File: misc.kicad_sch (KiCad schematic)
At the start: 12 parts, among them SW2001 SW_435441019830_SMD, SW2002 SW_435441019830_SMD, SW2003 SW_435441019830_SMD

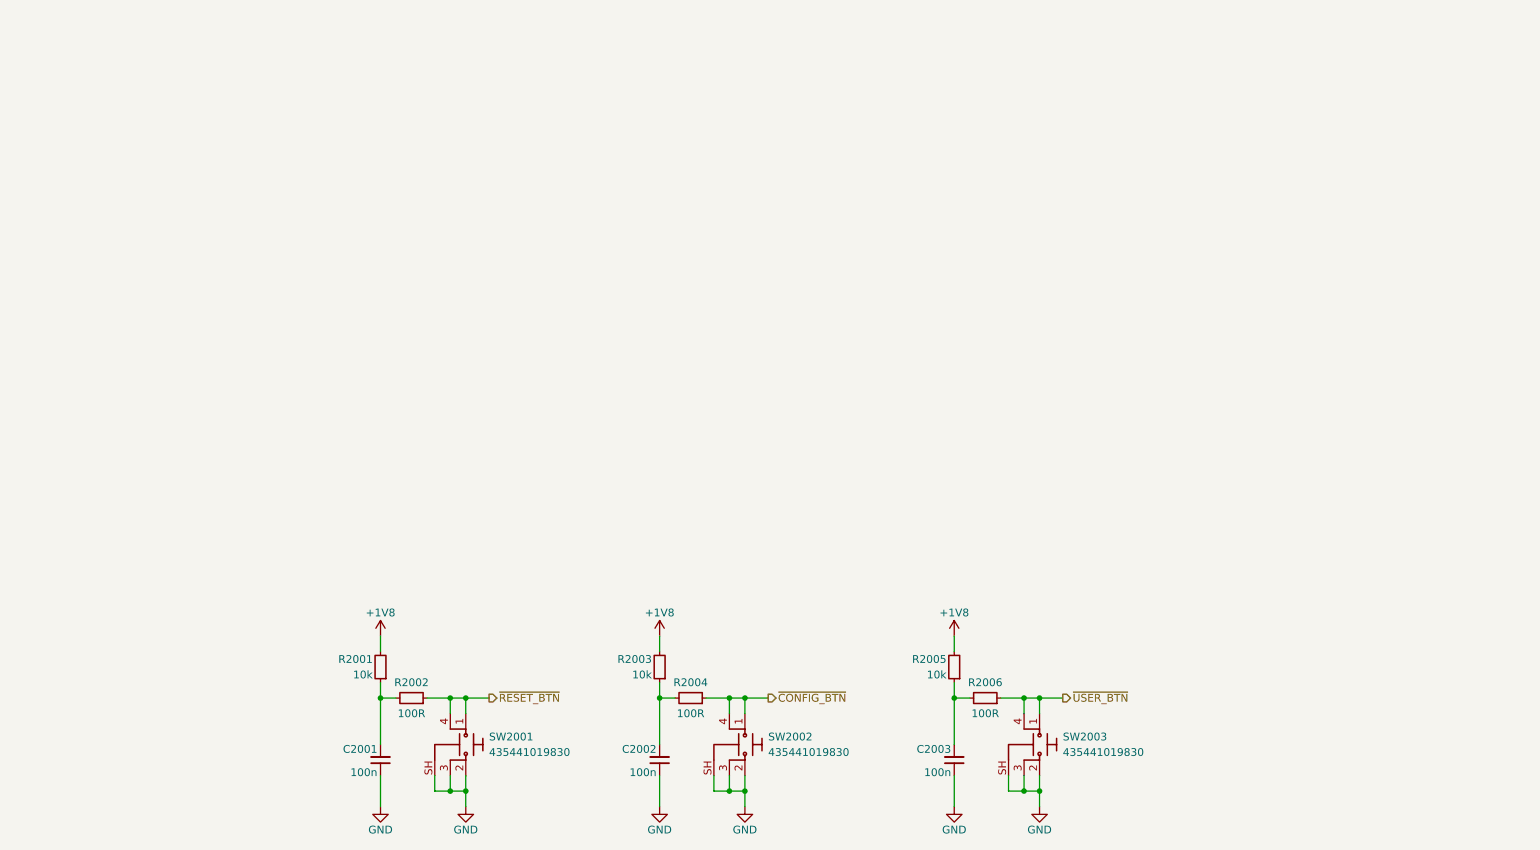
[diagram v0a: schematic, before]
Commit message: [#100125] Add DEBUG buttons, connect BIOS on root schematic
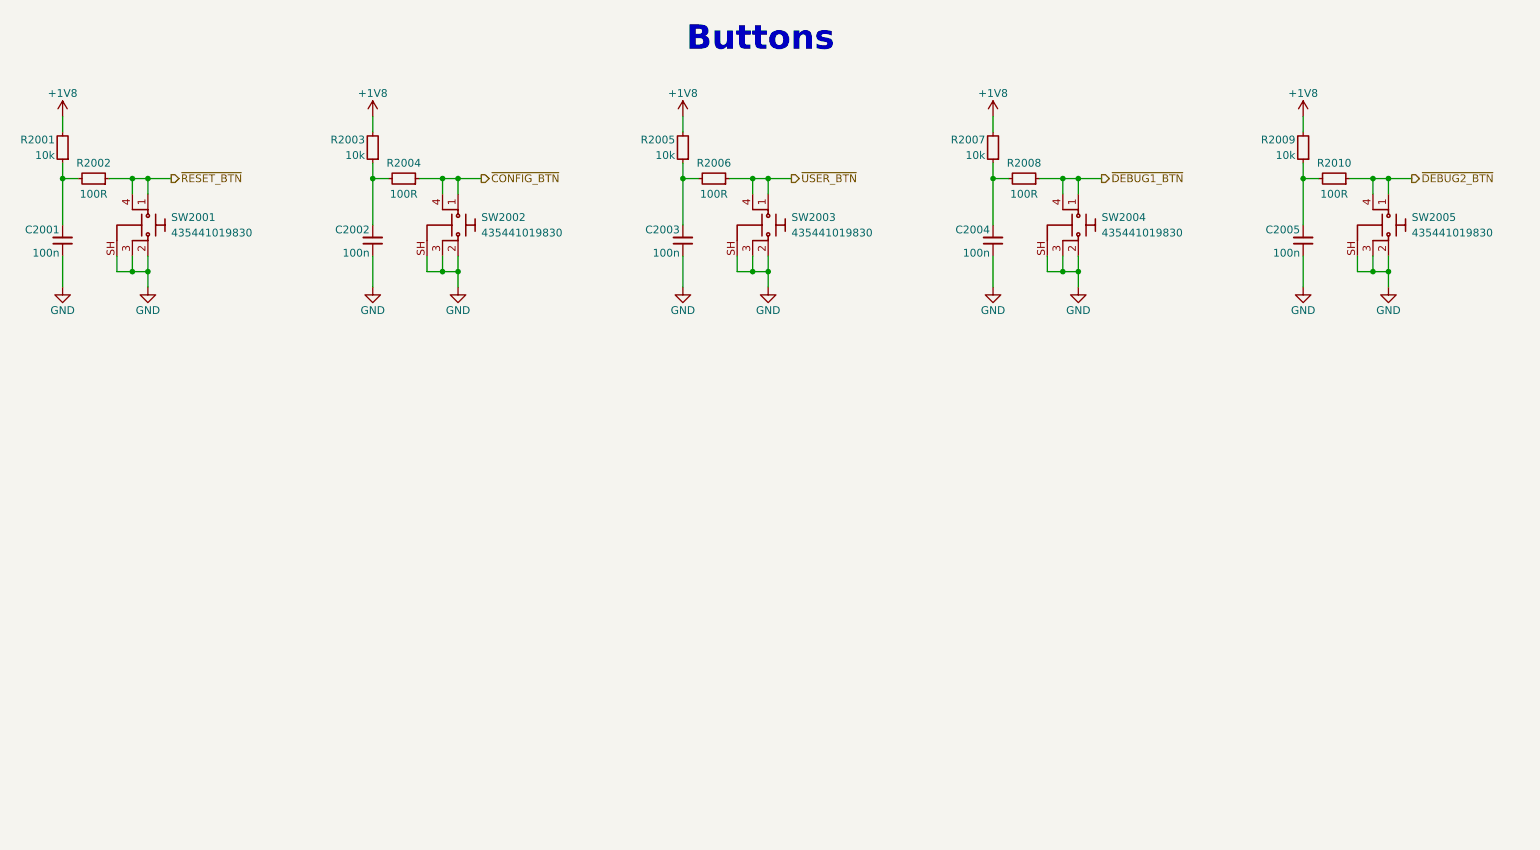
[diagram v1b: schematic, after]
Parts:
- added C2004, C2005: C_100n_0402, antmicro-footprints:C_0402_1005Metric, symbol antmicroCapacitors0402:C_100n_0402
- added R2007, R2009: R_10k_0402, antmicro-footprints:R_0402_1005Metric, symbol antmicroResistors0402:R_10k_0402
- added R2008, R2010: R_100R_0402, antmicro-footprints:R_0402_1005Metric, symbol antmicroResistors0402:R_100R_0402
- added SW2004, SW2005: SW_435441019830_SMD, antmicro-footprints:SW_435441019830_SMD, symbol antmicroPushbuttonSwitches:SW_435441019830_SMD
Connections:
- net +1V8: now also R2007.2, R2009.2
- net GND: now also C2004.1, C2005.1, SW2004.2, SW2004.3, SW2004.SH, SW2005.2, SW2005.3, SW2005.SH
- new net: C2005.2, R2009.1, R2010.2
- new net: C2004.2, R2007.1, R2008.2
- new net ~{DEBUG1_BTN}: R2008.1, SW2004.1, SW2004.4
- new net ~{DEBUG2_BTN}: R2010.1, SW2005.1, SW2005.4
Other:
- note added: "Buttons"
- moved on the sheet: C2001, C2002, C2003, R2001, R2002, R2003, R2004, R2005, R2006, SW2001, SW2002, SW2003

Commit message: [#100125] Add DEBUG LEDs
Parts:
- added D2001, D2002: LED_G_0402_VLMTG1500-GS08, antmicro-footprints:LED_0402_1005Metric_G, symbol antmicroLEDIndicationDiscrete:LED_G_0402_VLMTG1500-GS08
- added Q2001, Q2002: PJE138K, antmicro-footprints:SOT-523, symbol antmicroTransistorsFETsMOSFETsSingle:PJE138K
- added R2011, R2012: R_1k_0402, antmicro-footprints:R_0402_1005Metric, symbol antmicroResistors0402:R_1k_0402
- added R2013, R2014: R_10k_0402, antmicro-footprints:R_0402_1005Metric, symbol antmicroResistors0402:R_10k_0402
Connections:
- net GND: now also Q2001.2 (S), Q2002.2 (S), R2013.1, R2014.1
- new net: D2002.1 (C), Q2002.3 (D)
- new net: D2001.1 (C), Q2001.3 (D)
- new net: D2002.2 (A), R2012.1
- new net: D2001.2 (A), R2011.1
- new net +3V3: R2011.2, R2012.2
- new net ~{DEBUG_LED_1}: Q2001.1 (G), R2014.2
- new net ~{DEBUG_LED_2}: Q2002.1 (G), R2013.2
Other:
- note added: "Debug LEDs"

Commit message: [#100060] Add fan connector, connect misc sheet signals to SoM
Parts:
- added D2003: PMEG3010CEJ,115, antmicro-footprints:D_SOD-323F, symbol antmicroDiodesRectifiersSingle:PMEG3010CEJ,115
- added D2004: PESD5V0X1UB, antmicro-footprints:SOD-523, symbol antmicroTVSDiodes:PESD5V0X1UB
- added J2001: Molex_KK_1x2_22-23-2021, antmicro-footprints:Conn_Molex_KK_1x2_22-23-2021, symbol antmicroWire2BoardConnectors:Molex_KK_1x2_22-23-2021
- added Q2003: PJA3404, antmicro-footprints:SOT-23-3, symbol antmicroTransistorsFETsMOSFETsSingle:PJA3404
- added R2015: R_10k_0402, antmicro-footprints:R_0402_1005Metric, symbol antmicroResistors0402:R_10k_0402
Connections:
- net GND: now also D2004.2 (A), Q2003.2 (S), R2015.1
- new net: D2003.2 (A), J2001.2, Q2003.3 (D)
- new net +5V: D2003.1 (C), J2001.1
- new net FAN_EN: D2004.1 (C), Q2003.1 (G), R2015.2

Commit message: [#99649] Fix HS connector rule area, add DP AUX, HPD and CONFIG pins to DP bus, connect most signals on root schematic
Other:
- note added: "Fan connector"
- moved on the sheet: D2003, D2004, J2001, Q2003, R2015

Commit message: [#100282] Reorder schematic pages, reannotate schematic
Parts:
- renumbered C2001 to C2101, C2002 to C2102, C2003 to C2103, C2004 to C2104, C2005 to C2105, D2001 to D2101, D2002 to D2102, D2003 to D2103, D2004 to D2104, J2001 to J2101, Q2001 to Q2101, Q2002 to Q2102, Q2003 to Q2103, R2001 to R2101, R2003 to R2102, R2005 to R2103, R2007 to R2104, R2009 to R2105, R2002 to R2106, R2004 to R2107, R2006 to R2108, R2008 to R2109, R2010 to R2110, R2011 to R2111, R2012 to R2112, R2014 to R2113, R2013 to R2114, R2015 to R2115, SW2001 to SW2101, SW2002 to SW2102, SW2003 to SW2103, SW2004 to SW2104, SW2005 to SW2105

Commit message: [#100282] Swap TMP default from QSPI to SPI, add level shifter for PECI I2C bus, connect user button
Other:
- moved on the sheet: C2101, C2102, C2103, C2104, C2105, D2101, D2102, D2103, D2104, J2101, Q2101, Q2102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
